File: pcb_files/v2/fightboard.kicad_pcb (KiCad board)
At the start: 2 copper layers, 179 x 60 mm, 39 parts, among them J1 SW_Push, K1 SW_Push, M1 XIAO-RP2040, P1 SW_Push, U1 SW_Push

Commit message: update v2 pcb
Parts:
- removed C104: C_Small, Resistor_SMD:R_2010_5025Metric_Pad1.40x2.65mm_HandSolder
- removed LD1: SN74AHCT125D, kb_lib:SOIC127P600X175-14N
- removed the REF** at (85.0, 39.0)
- removed the REF** at (187.0, 39.0)
- added C1: C_Small, Resistor_SMD:R_2010_5025Metric_Pad1.40x2.65mm_HandSolder, B.Cu at (165.6, 49.0)
- added C10: C_Small, Resistor_SMD:R_2010_5025Metric_Pad1.40x2.65mm_HandSolder, B.Cu at (87.0, 77.0)
- added C11: C_Small, Resistor_SMD:R_2010_5025Metric_Pad1.40x2.65mm_HandSolder, B.Cu at (66.0, 77.0)
- added C12: C_Small, Resistor_SMD:R_2010_5025Metric_Pad1.40x2.65mm_HandSolder, B.Cu at (100.0, 56.0)
- added C13: C_Small, Resistor_SMD:R_2010_5025Metric_Pad1.40x2.65mm_HandSolder, B.Cu at (102.0, 48.0)
- added C2: C_Small, Resistor_SMD:R_2010_5025Metric_Pad1.40x2.65mm_HandSolder, B.Cu at (186.0, 49.0)
- added C3: C_Small, Resistor_SMD:R_2010_5025Metric_Pad1.40x2.65mm_HandSolder, B.Cu at (207.0, 49.0)
- added C4: C_Small, Resistor_SMD:R_2010_5025Metric_Pad1.40x2.65mm_HandSolder, B.Cu at (226.0, 49.0)
- added C5: C_Small, Resistor_SMD:R_2010_5025Metric_Pad1.40x2.65mm_HandSolder, B.Cu at (213.0, 77.0)
- added C6: C_Small, Resistor_SMD:R_2010_5025Metric_Pad1.40x2.65mm_HandSolder, B.Cu at (192.0, 77.0)
- added C7: C_Small, Resistor_SMD:R_2010_5025Metric_Pad1.40x2.65mm_HandSolder, B.Cu at (171.0, 77.0)
- added C8: C_Small, Resistor_SMD:R_2010_5025Metric_Pad1.40x2.65mm_HandSolder, B.Cu at (150.0, 77.0)
- added C9: C_Small, Resistor_SMD:R_2010_5025Metric_Pad1.40x2.65mm_HandSolder, B.Cu at (108.0, 77.0)
- added G***: LOGO, kb_lib:favicon, F.Cu at (209.0, 39.0)
- added G***: LOGO, kb_lib:qmk_logo, F.Cu at (165.0, 39.0)
- added G***: LOGO, kb_lib:ez, B.Cu at (72.0, 47.0)
- added LED13: WS2812B, kb_lib:Reverse Mount SK6812MINI-E, F.Cu at (96.0, 45.0)
- added LS1: TXB0108PWR, kb_lib:SOP65P640X120-20N, B.Cu at (111.0, 41.0)
- added REF**: MountingHole_2.7mm, MountingHole:MountingHole_2.7mm, F.Cu at (187.0, 38.0)
- added REF**: MountingHole_2.7mm, MountingHole:MountingHole_2.7mm, F.Cu at (85.0, 37.9)
- renumbered ;1 to ;, A1 to A, BKSP1 to BKSP, D1 to D, ESC1 to ENTER, I1 to I, IOEX2 to IOEX1, J1 to J, K1 to K, L1 to L, LED0 to LED, MNUS1 to MINUS, O1 to O, P1 to P, PLUS1 to PLUS, S1 to S, U1 to U, W1 to W
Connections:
- LED12 pad 2: unconnected-(LED12-Pad2) -> Net-(LED12-Pad2)
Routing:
- net Net-(LED1-Pad1): track 418.8 -> 471.5 mm, vias 10 -> 20
- net Net-(;1-Pad1): track 631.4 -> 680.6 mm, vias 8 -> 10
- net Net-(IOEX1-Pad10): track 40.0 -> 84.7 mm
- net Net-(R330-Pad2): track 25.5 -> 41.7 mm, vias 0 -> 2
- net Net-(LED12-Pad2): track 0.00 -> 7.58 mm
- net Net-(A1-Pad2): track 79.8 -> 84.6 mm
- net Net-(ENT1-Pad2): track 133.2 -> 129.0 mm
- net Net-(IOEX1-Pad17): track 31.6 -> 34.4 mm
- net Net-(IOEX1-Pad9): track 75.0 -> 73.0 mm
- net Net-(IOEX1-Pad2): track 35.0 -> 33.2 mm
- net Net-(IOEX1-Pad8): track 53.4 -> 51.8 mm
- net Net-(IOEX1-Pad14): track 57.8 -> 59.2 mm, vias 1 -> 2
- net Net-(I1-Pad2): track 31.9 -> 30.5 mm
- net Net-(M1-Pad1): track 10.5 -> 9.29 mm
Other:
- board text added: "FIGHTBOARD v2"
- board text added: "PCB/Firmware by Cartex10 Firmware built using QMK"
- board text added: "When in doubt, wake-up DP"

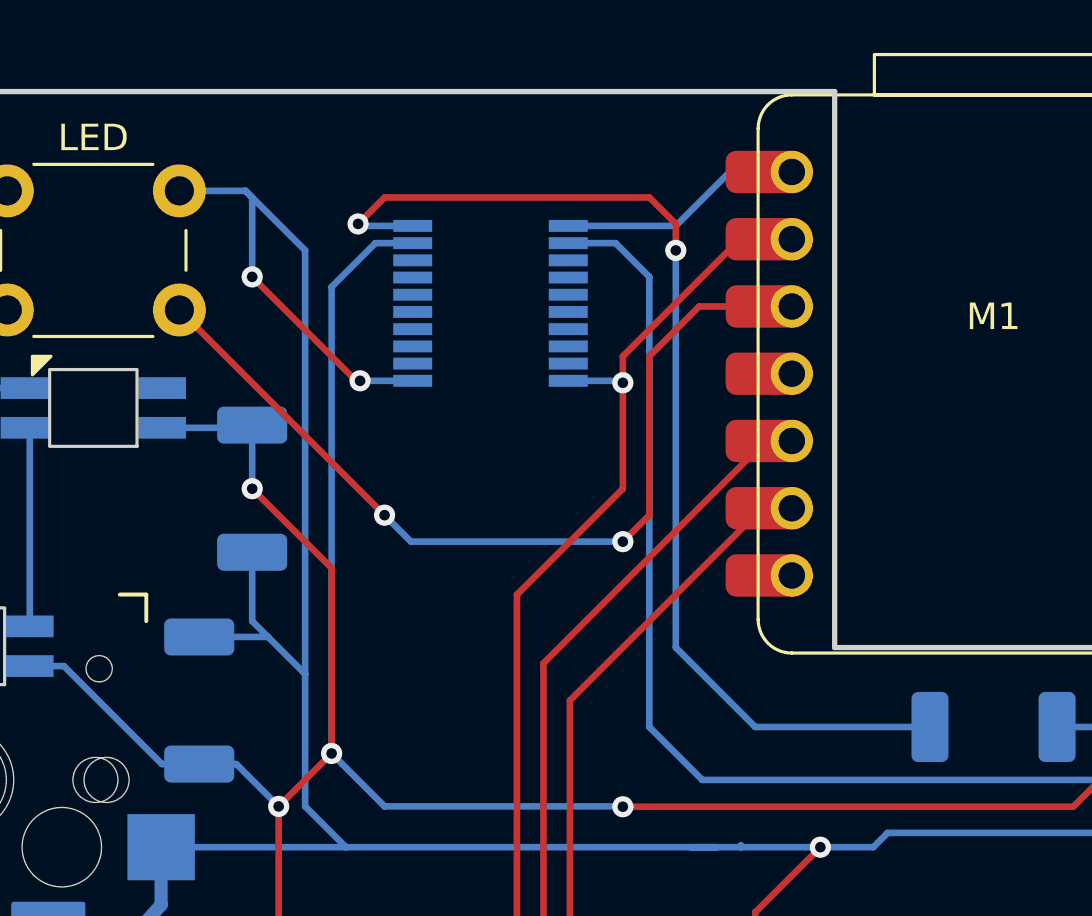
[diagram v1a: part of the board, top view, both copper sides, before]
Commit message: update pcb with led extension pins
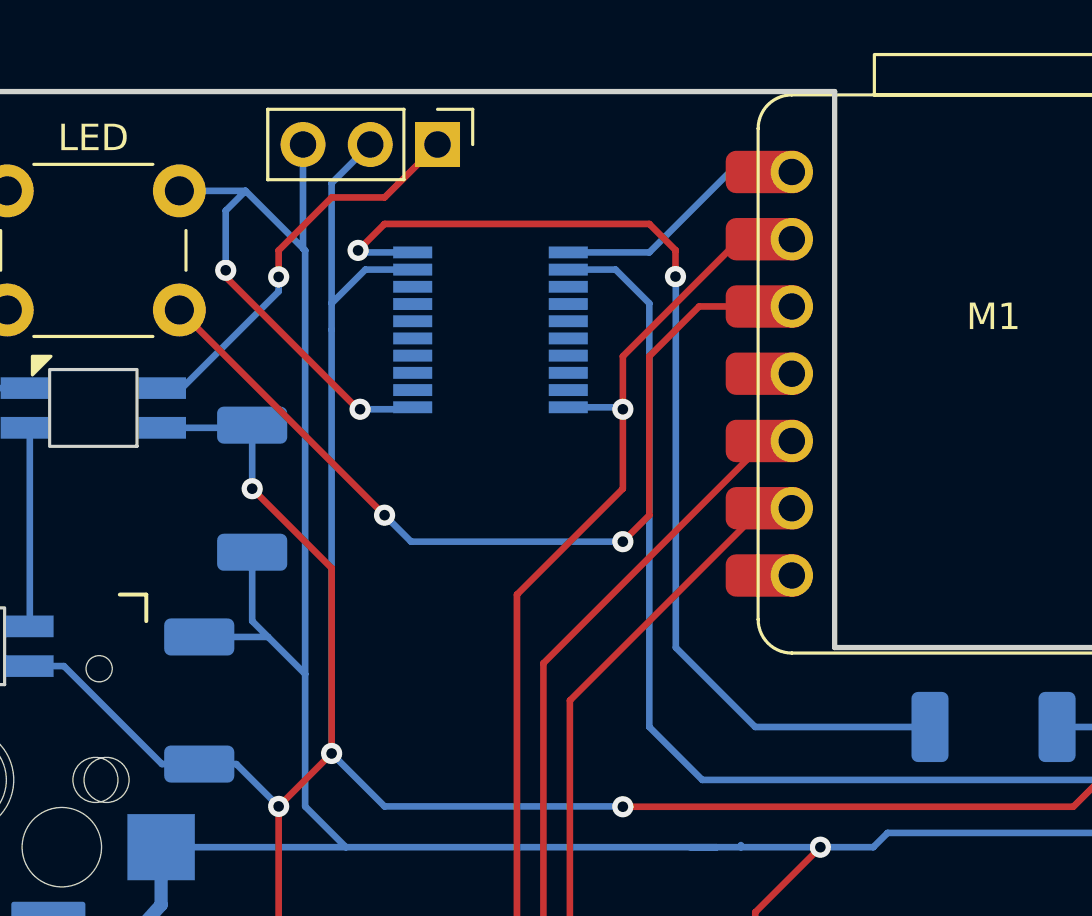
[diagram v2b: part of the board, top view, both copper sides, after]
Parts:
- added REF**: PinHeader_1x03_P2.54mm_Vertical, Connector_PinHeader_2.54mm:PinHeader_1x03_P2.54mm_Vertical, F.Cu at (109.0, 35.0)
- moved LS1 1.00 mm to (111.0, 42.0)
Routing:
- net unconnected-(LED13-Pad2): track 0.00 -> 15.1 mm, vias 0 -> 1
- net Net-(LED1-Pad1): track 471.5 -> 477.3 mm
- net Net-(;1-Pad1): track 680.6 -> 686.2 mm
- net Net-(IOEX1-Pad10): track 84.7 -> 83.7 mm
- net Net-(R330-Pad2): track 41.7 -> 40.8 mm
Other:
- board text added: "5V"
- board text added: "DOUT"
- board text added: "GND"

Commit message: fix errors with pcb
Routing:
- net Net-(LED1-Pad1): track 477.3 -> 481.9 mm, vias 20 -> 22
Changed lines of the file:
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@@
   (segment (start 144 49) (end 144 46) (width 0.25) (layer "F.Cu") (net 19))
   (segment (start 160 47) (end 165 47) (width 0.25) (layer "F.Cu") (net 19))
+  (segment (start 69 74) (end 70 73) (width 0.25) (layer "F.Cu") (net 19))
   (segment (start 206 47) (end 226 47) (width 0.25) (layer "F.Cu") (net 19))
   (segment (start 144 46) (end 144 44) (width 0.25) (layer "F.Cu") (net 19))
   (segment (start 228 49) (end 228 52) (width 0.25) (layer "F.Cu") (net 19))
   (segment (start 181 47) (end 185 47) (width 0.25) (layer "F.Cu") (net 19))
+  (segment (start 70 73) (end 71 73) (width 0.25) (layer "F.Cu") (net 19))
   (segment (start 144 44) (end 144 38) (width 0.25) (layer "F.Cu") (net 19))
   (segment (start 165 47) (end 181 47) (width 0.25) (layer "F.Cu") (net 19))
@@
   (via (at 227 55) (size 0.8) (drill 0.4) (layers "F.Cu" "B.Cu") (net 19))
   (via (at 185 47) (size 0.8) (drill 0.4) (layers "F.Cu" "B.Cu") (net 19))
+  (via (at 71 73) (size 0.8) (drill 0.4) (layers "F.Cu" "B.Cu") (net 19))
   (via (at 116 60.012299) (size 0.8) (drill 0.4) (layers "F.Cu" "B.Cu") (net 19))
   (via (at 226 47) (size 0.8) (drill 0.4) (layers "F.Cu" "B.Cu") (net 19))
@@
   (via (at 203 50) (size 0.8) (drill 0.4) (layers "F.Cu" "B.Cu") (net 19))
   (via (at 105 58) (size 0.8) (drill 0.4) (layers "F.Cu" "B.Cu") (net 19))
+  (via (at 69 74) (size 0.8) (drill 0.4) (layers "F.Cu" "B.Cu") (net 19))
   (via (at 182 50) (size 0.8) (drill 0.4) (layers "F.Cu" "B.Cu") (net 19))
   (via (at 181 56) (size 0.8) (drill 0.4) (layers "F.Cu" "B.Cu") (net 19))
@@
   (segment (start 224 49) (end 223.6 49) (width 0.25) (layer "B.Cu") (net 19))
   (segment (start 150.3 74.3) (end 156.4 74.3) (width 0.25) (layer "B.Cu") (net 19))
+  (segment (start 66 74.6) (end 68.4 74.6) (width 0.25) (layer "B.Cu") (net 19))
   (segment (start 193.3 74.3) (end 193 74.6) (width 0.25) (layer "B.Cu") (net 19))
   (segment (start 156.6 54.7) (end 157.9 56) (width 0.25) (layer "B.Cu") (net 19))
@@
   (segment (start 214.3 74.3) (end 214 74.6) (width 0.25) (layer "B.Cu") (net 19))
   (segment (start 170.6 74.6) (end 169 73) (width 0.25) (layer "B.Cu") (net 19))
-  (segment (start 72.4 73.6) (end 74 72) (width 0.25) (layer "B.Cu") (net 19))
   (segment (start 206 47.6) (end 206 47) (width 0.25) (layer "B.Cu") (net 19))
   (segment (start 183 49) (end 182 50) (width 0.25) (layer "B.Cu") (net 19))
@@
   (segment (start 192 74.6) (end 191.6 74.6) (width 0.25) (layer "B.Cu") (net 19))
   (segment (start 152 73) (end 150.4 74.6) (width 0.25) (layer "B.Cu") (net 19))
+  (segment (start 68.4 74.6) (end 69 74) (width 0.25) (layer "B.Cu") (net 19))
   (segment (start 150.4 74.6) (end 150 74.6) (width 0.25) (layer "B.Cu") (net 19))
   (segment (start 105 42) (end 105 41) (width 0.25) (layer "B.Cu") (net 19))
@@
   (segment (start 87 74.6) (end 87.3 74.3) (width 0.25) (layer "B.Cu") (net 19))
   (segment (start 177.4 74.3) (end 171.3 74.3) (width 0.25) (layer "B.Cu") (net 19))
+  (segment (start 71 73) (end 71.1 73) (width 0.25) (layer "B.Cu") (net 19))
   (segment (start 163.2 49) (end 162 49) (width 0.25) (layer "B.Cu") (net 19))
   (segment (start 157.9 56) (end 160 56) (width 0.25) (layer "B.Cu") (net 19))
@@
   (segment (start 198.6 54.7) (end 199.9 56) (width 0.25) (layer "B.Cu") (net 19))
   (segment (start 223 49) (end 222 50) (width 0.25) (layer "B.Cu") (net 19))
-  (segment (start 72.4 74.3) (end 72.4 73.6) (width 0.25) (layer "B.Cu") (net 19))
   (segment (start 95 72) (end 84 72) (width 0.25) (layer "B.Cu") (net 19))
   (segment (start 211 73) (end 194 73) (width 0.25) (layer "B.Cu") (net 19))
@@
   (segment (start 150 74.6) (end 150.3 74.3) (width 0.25) (layer "B.Cu") (net 19))
   (segment (start 220.9 56) (end 223 56) (width 0.25) (layer "B.Cu") (net 19))
+  (segment (start 71.1 73) (end 72.4 74.3) (width 0.25) (layer "B.Cu") (net 19))
   (segment (start 107 60) (end 115.987701 60) (width 0.25) (layer "B.Cu") (net 19))
   (segment (start 87.3 74.3) (end 93.4 74.3) (width 0.25) (layer "B.Cu") (net 19))
